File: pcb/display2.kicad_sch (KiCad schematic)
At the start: 20 parts, among them Q5 DMG2301L, Q6 DMG2301L, Q7 DMG2301L, Q8 DMG2301L, U3 TPIC6C596

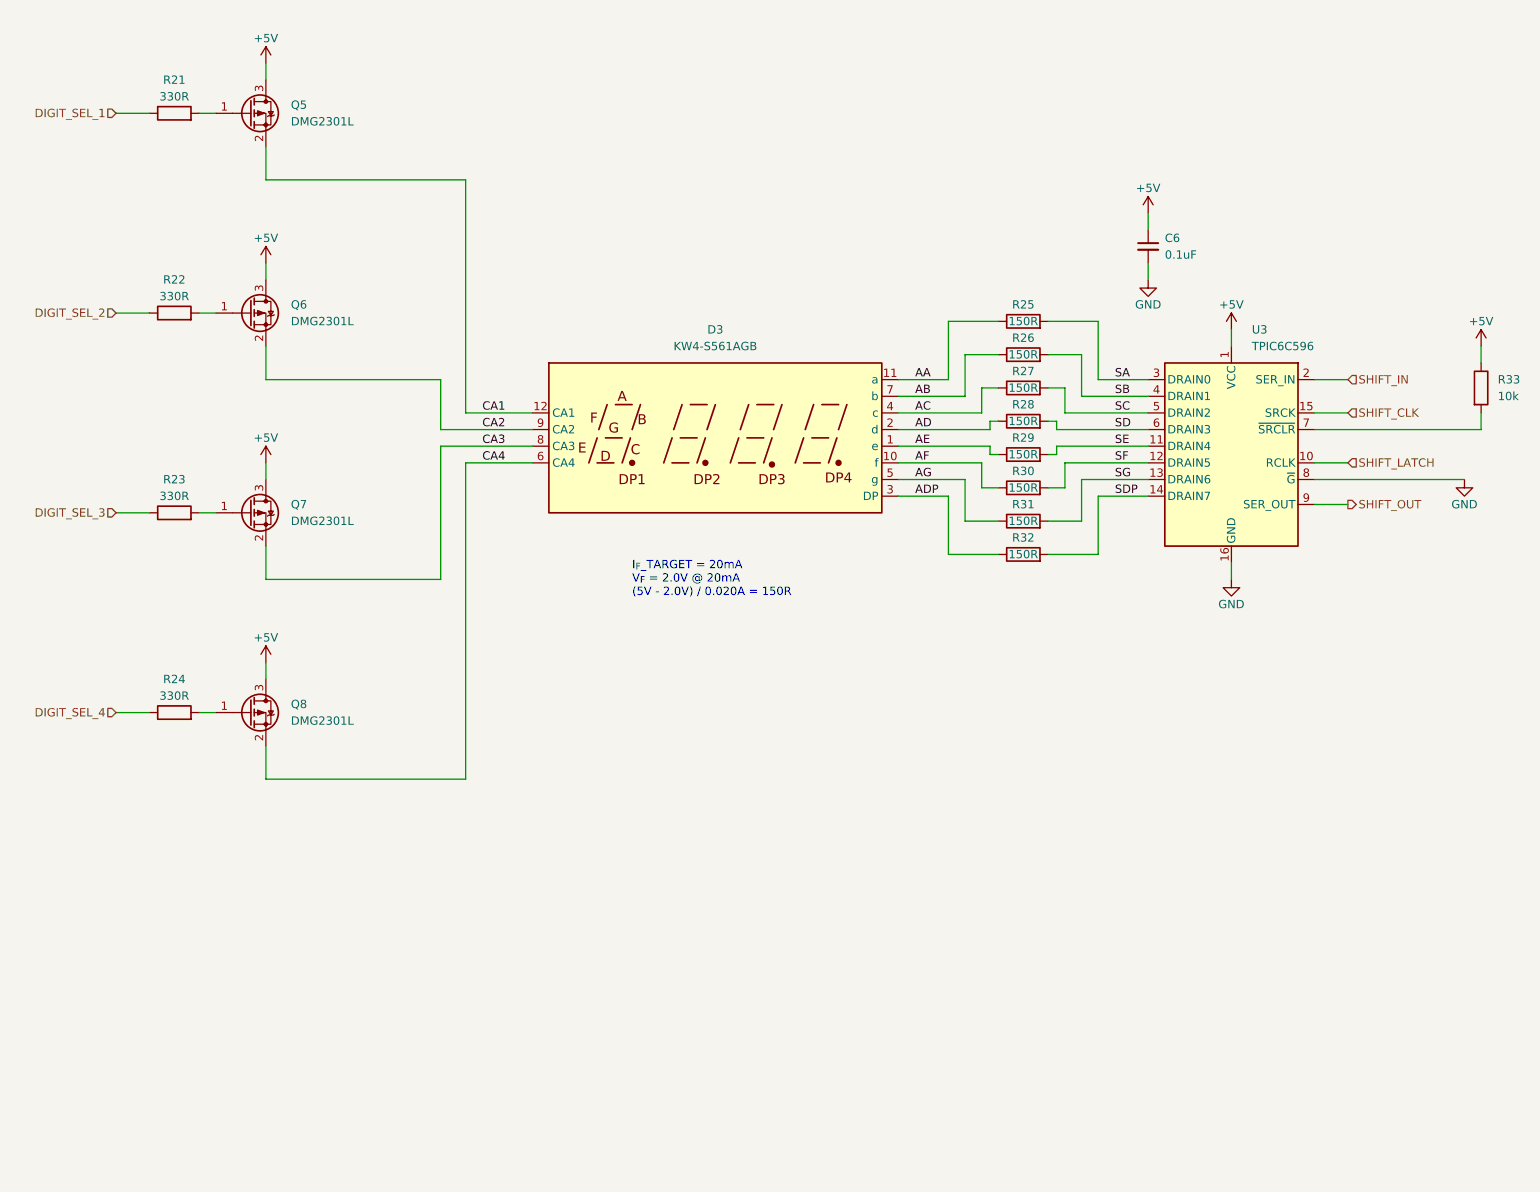
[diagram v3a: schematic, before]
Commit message: start to route display traces
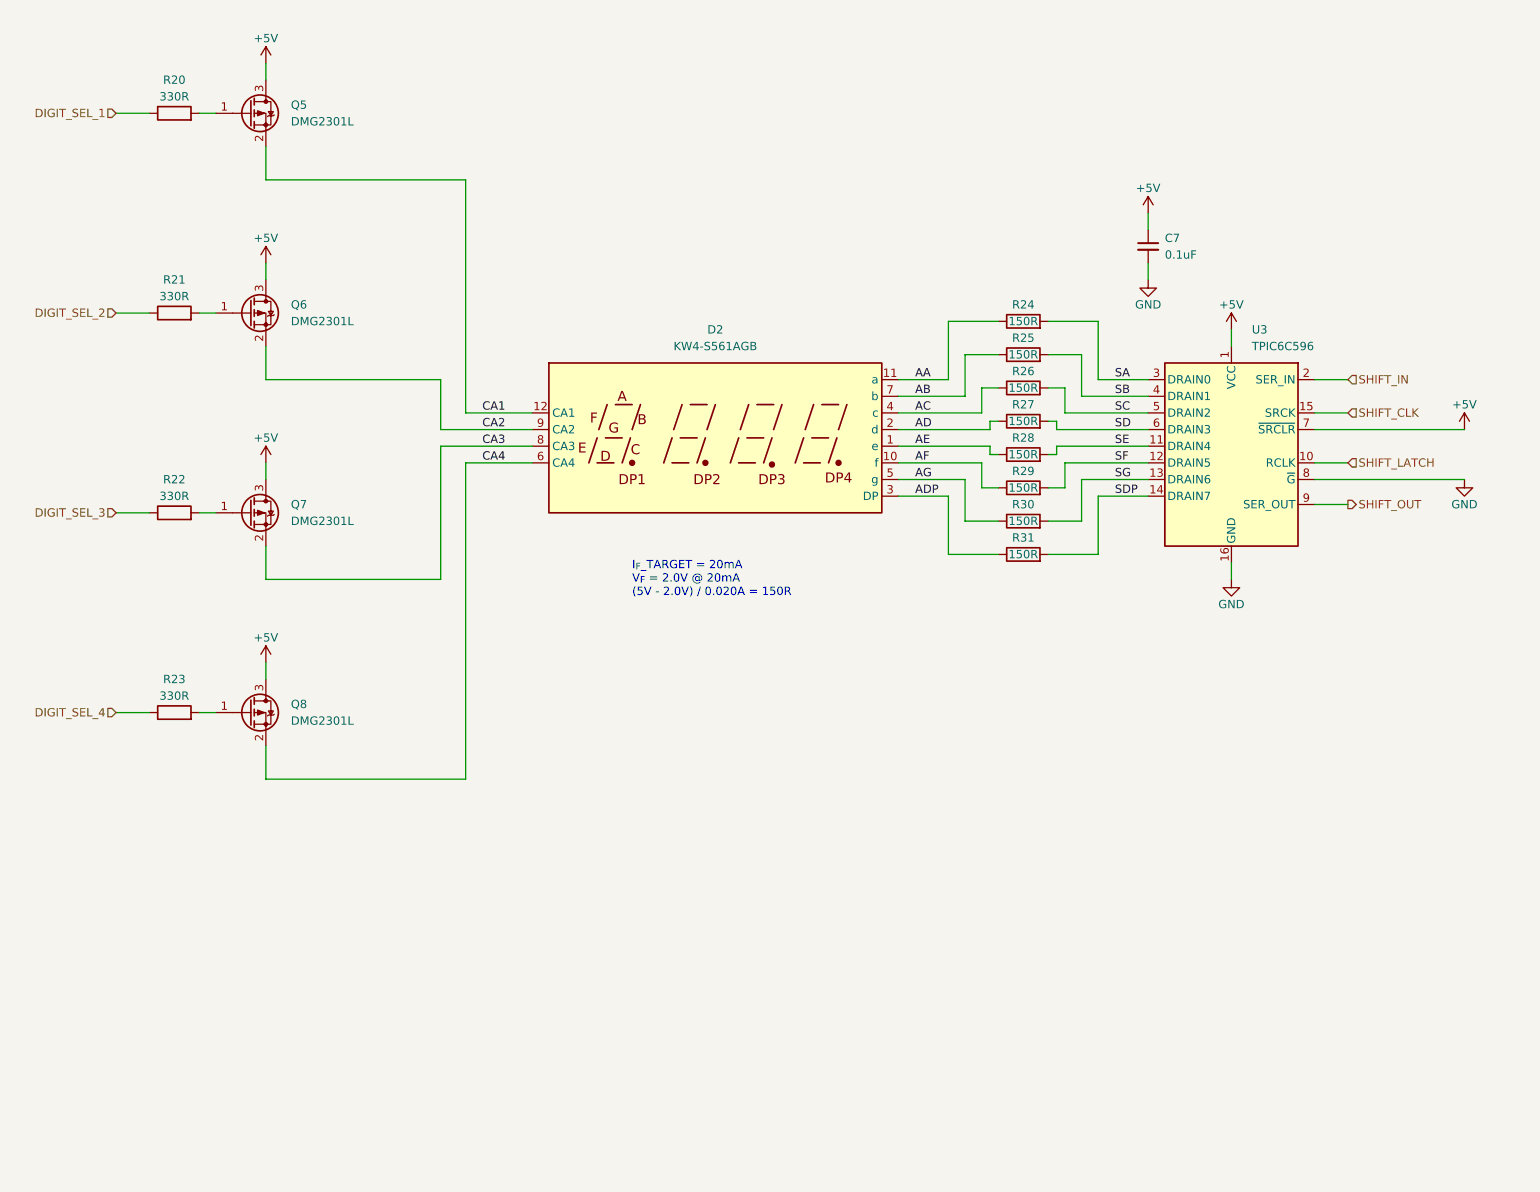
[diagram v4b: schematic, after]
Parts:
- removed R33: 10k, Resistor_SMD:R_0805_2012Metric_Pad1.20x1.40mm_HandSolder, symbol Device:R
- renumbered C6 to C7, D3 to D2, R21 to R20, R22 to R21, R23 to R22, R24 to R23, R25 to R24, R26 to R25, R27 to R26, R28 to R27, R29 to R28, R30 to R29, R31 to R30, R32 to R31
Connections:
- net +5V: now also U3.7 (~{SRCLR})

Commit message: continue layout. improve 3d model
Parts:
- D2: footprint mtg_life_counter:KW4-S561xxB_SMD -> mtg_life_counter:KW4-S561xGB_SMD
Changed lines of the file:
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@@
 			)
 		)
-		(property "Footprint" "mtg_life_counter:KW4-S561xxB_SMD"
+		(property "Footprint" "mtg_life_counter:KW4-S561xGB_SMD"
 			(at 132.08 95.25 0)
 			(effects

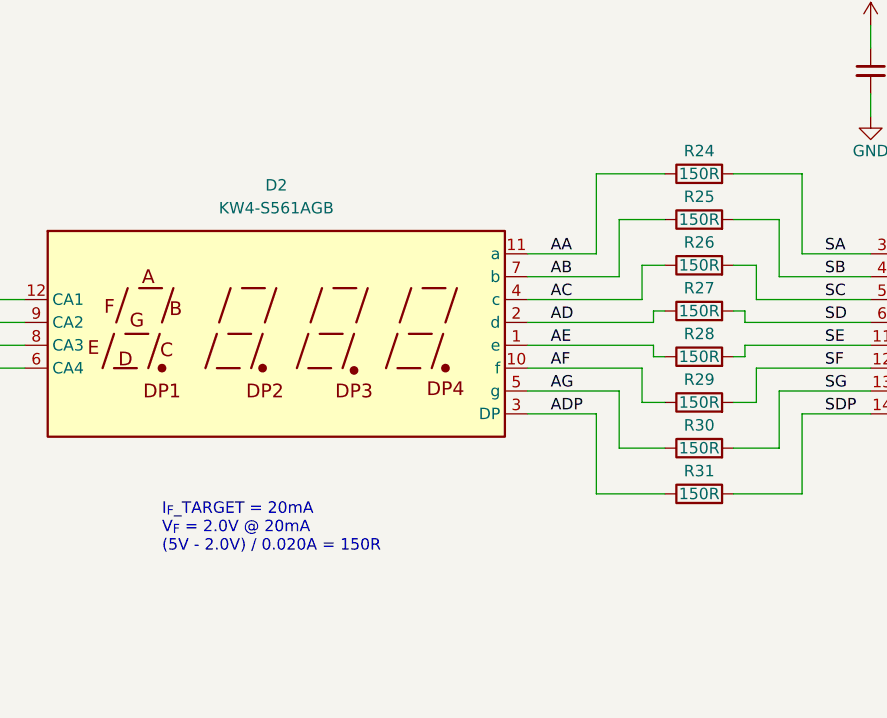
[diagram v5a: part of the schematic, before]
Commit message: continue layout. update leds for KD4 led modules
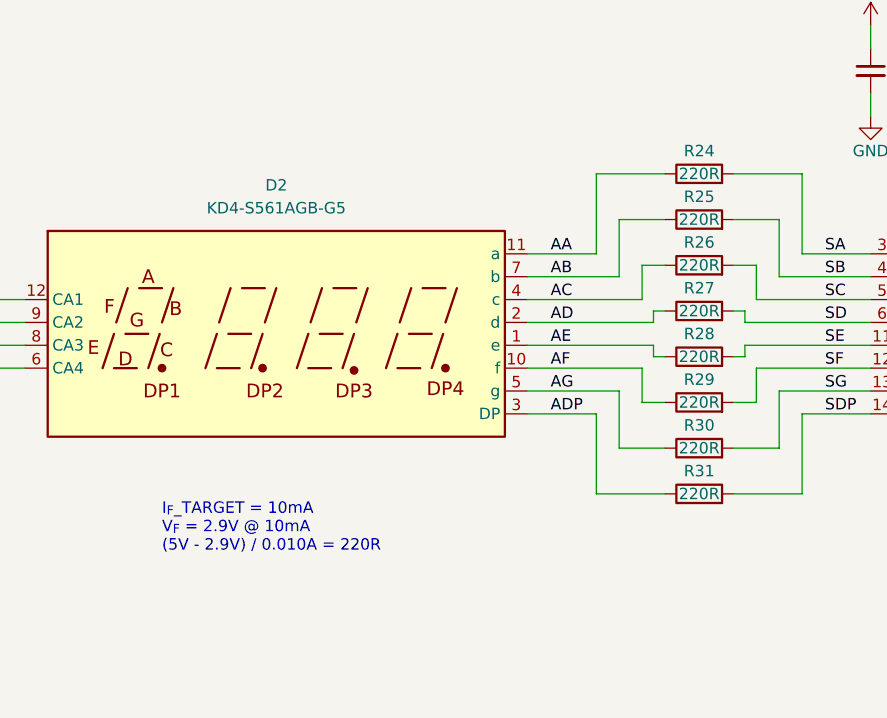
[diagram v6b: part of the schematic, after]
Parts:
- D2: value KW4-S561AGB -> KD4-S561AGB-G5; footprint mtg_life_counter:KW4-S561xGB_SMD -> mtg_life_counter:KD4-S561xxB_SMD_Slim
- R24, R25, R26, R27, R28, R29, R30, R31: value 150R -> 220R
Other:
- note added: "I_{F}_TARGET = 10mA V_{F} = 2.9V @ 10mA (5V - 2.9V) / 0.010A = 220R"
- note removed: "I_{F}_TARGET = 20mA V_{F} = 2.0V @ 20mA (5V - 2.0V) / 0.020A = 150R"
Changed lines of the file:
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@@
 		(company "Max Proskauer")
 	)
-	(text "I_{F}_TARGET = 20mA\nV_{F} = 2.0V @ 20mA\n(5V - 2.0V) / 0.020A = 150R"
+	(text "I_{F}_TARGET = 10mA\nV_{F} = 2.9V @ 10mA\n(5V - 2.9V) / 0.010A = 220R"
 		(exclude_from_sim no)
 		(at 119.38 104.14 0)
@@
 			)
 		)
-		(property "Value" "150R"
+		(property "Value" "220R"
 			(at 179.07 74.93 90)
 			(effects
@@
 			)
 		)
-		(property "Value" "150R"
+		(property "Value" "220R"
 			(at 179.07 90.17 90)
 			(effects
@@
 			)
 		)
-		(property "Value" "150R"
+		(property "Value" "220R"
 			(at 179.07 100.33 90)
 			(effects
@@
 			)
 		)
-		(property "Value" "150R"
+		(property "Value" "220R"
 			(at 179.07 85.09 90)
 			(effects
@@
 			)
 		)
-		(property "Value" "150R"
+		(property "Value" "220R"
 			(at 179.07 95.25 90)
 			(effects
@@
 			)
 		)
-		(property "Value" "150R"
+		(property "Value" "220R"
 			(at 179.07 80.01 90)
 			(effects
@@
 			)
 		)
-		(property "Value" "150R"
+		(property "Value" "220R"
 			(at 179.07 69.85 90)
 			(effects
@@
 			)
 		)
-		(property "Value" "KW4-S561AGB"
+		(property "Value" "KD4-S561AGB-G5"
 			(at 132.08 68.58 0)
 			(effects
@@
 			)
 		)
-		(property "Footprint" "mtg_life_counter:KW4-S561xGB_SMD"
+		(property "Footprint" "mtg_life_counter:KD4-S561xxB_SMD_Slim"
 			(at 132.08 95.25 0)
 			(effects
@@
 			)
 		)
-		(property "Value" "150R"
+		(property "Value" "220R"
 			(at 179.07 64.77 90)
 			(effects
